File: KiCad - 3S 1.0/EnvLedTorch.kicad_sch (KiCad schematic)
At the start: 64 parts, among them J1 USB_C_Receptacle_USB2.0, J101 Conn_01x02, J102 Conn_01x02, Q1 BSP89, Q2 BSP89, Q3 BSP89, Q4 AO3401A, Q5 AO3401A, SW101 SW_SPST, U1 HY2213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

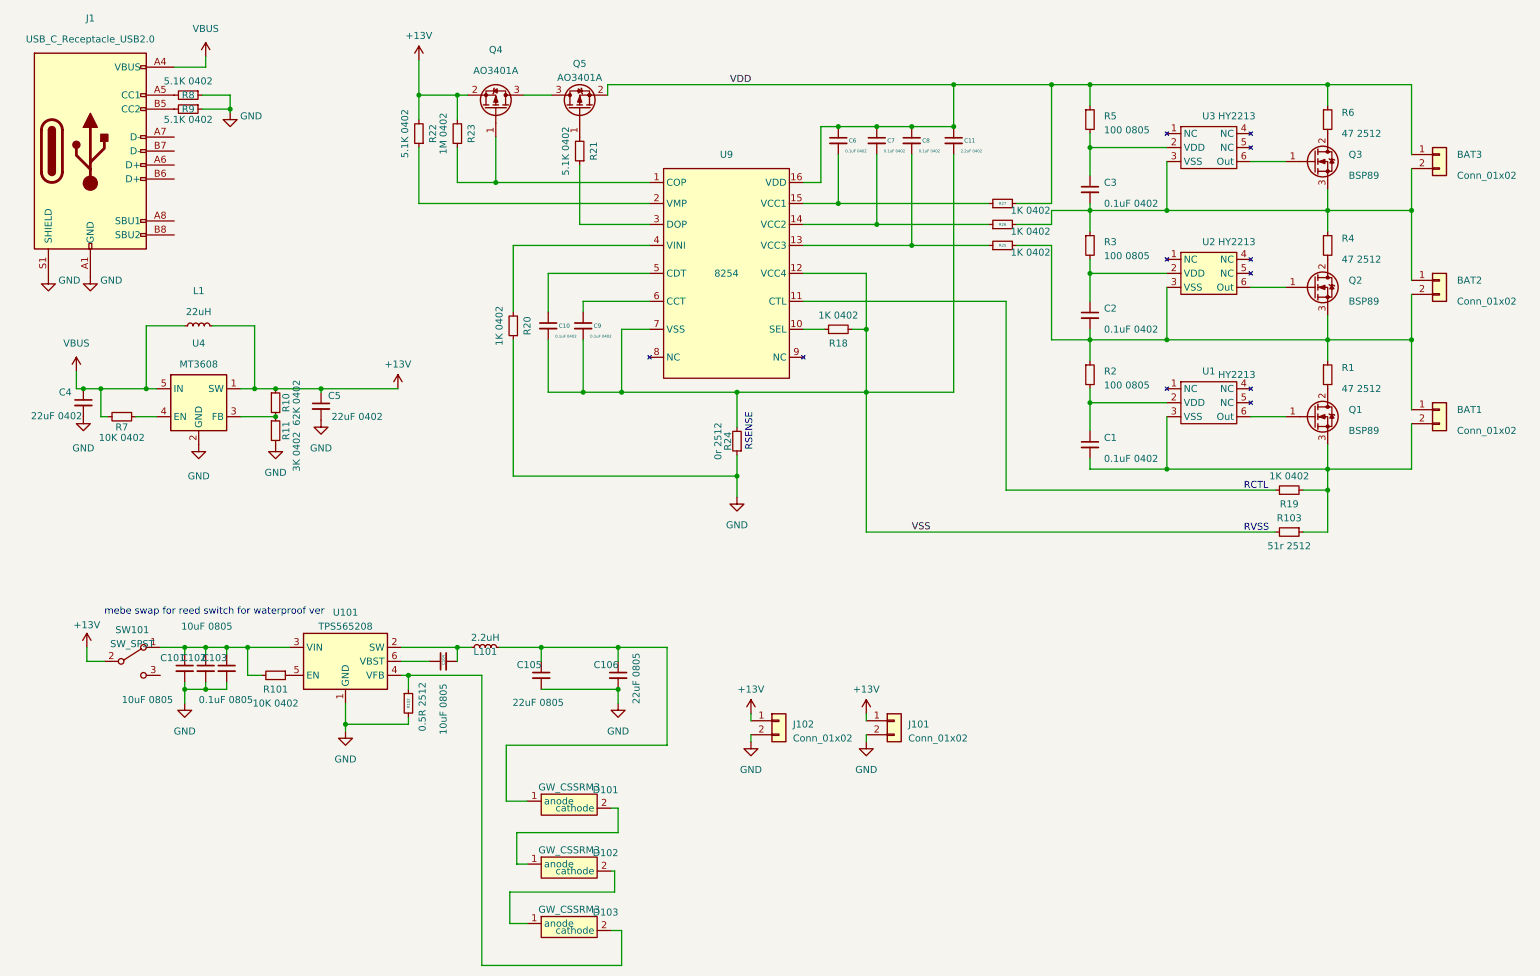
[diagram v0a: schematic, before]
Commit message: created lower cost single cell variant with less leds, this version will draw 1.2A possibly more due to losses and what not but can charge at 1.5A
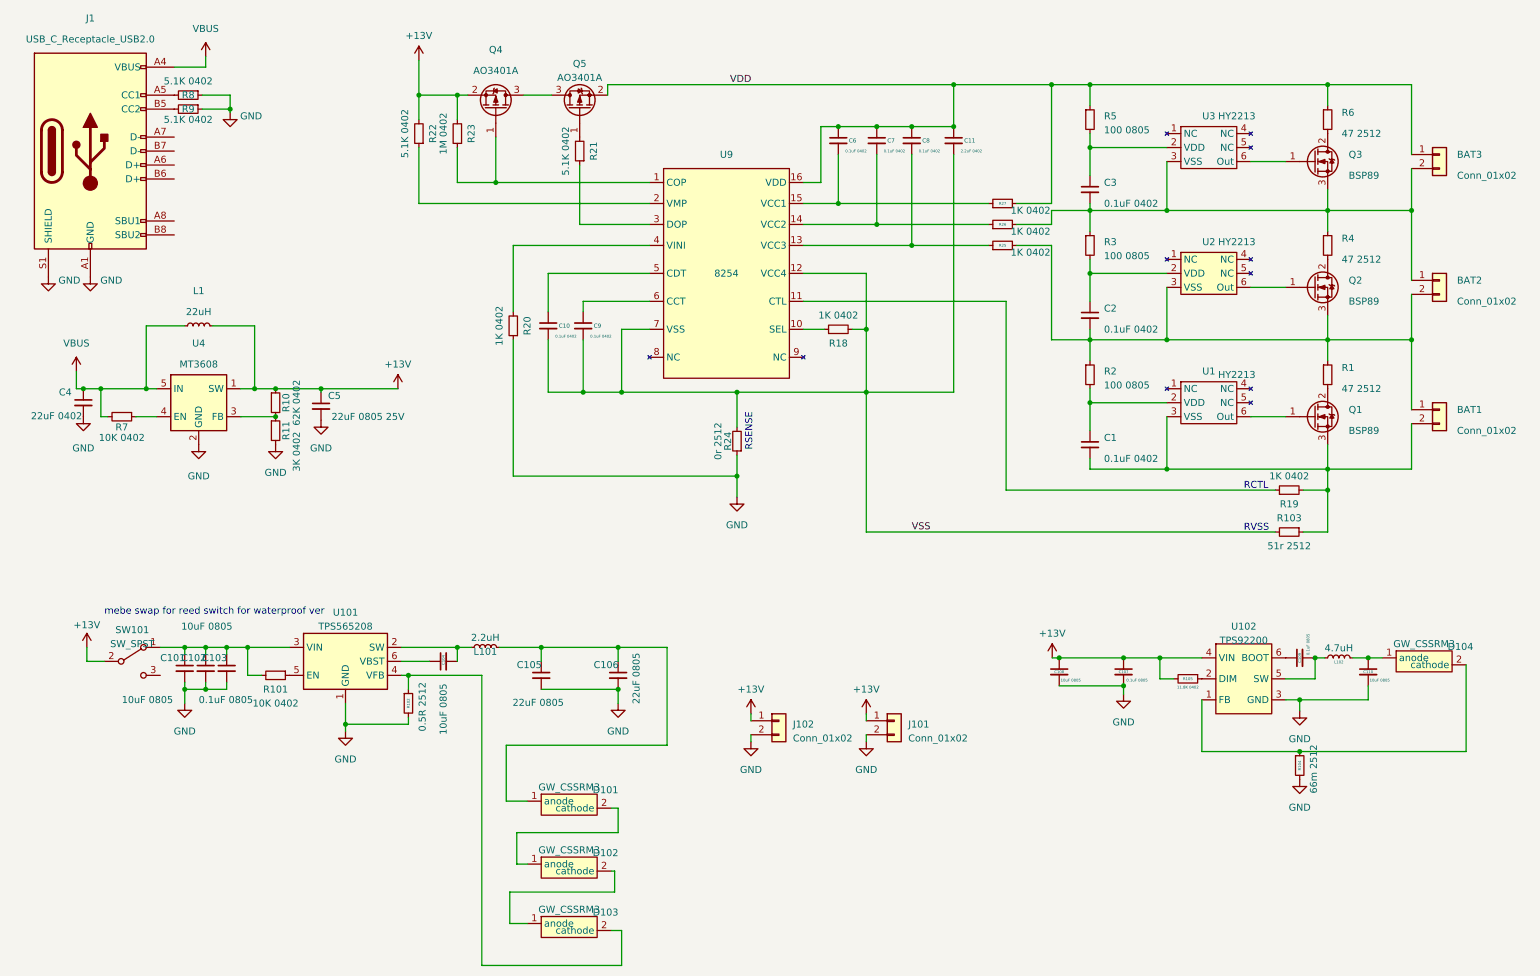
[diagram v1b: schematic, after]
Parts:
- added C107, C109: 0.1uF 0805, Capacitor_SMD:C_0805_2012Metric, symbol Device:C_Small
- added C108, C110: 10uF 0805, Capacitor_SMD:C_0805_2012Metric, symbol Device:C_Small
- added D104: GW_CSSRM3, GW_CSSRM3:GW_CSSRM3, symbol GW CSSRM3:GW_CSSRM3
- added L102: 4.7uH, Inductor_SMD:L_Sunlord_MWSA0402S, symbol Device:L_Small
- added R104: 66m 2512, Resistor_SMD:R_2512_6332Metric, symbol Device:R_Small
- added R105: 11.8K 0402, Resistor_SMD:R_0402_1005Metric, symbol Device:R_Small
- added U102: TPS92200, Package_TO_SOT_SMD:SOT-23-6, symbol TPS92200:TPS92200
- C5: value 22uF 0402 -> 22uF 0805 25V; footprint Capacitor_SMD:C_0402_1005Metric -> Capacitor_SMD:C_0805_2012Metric
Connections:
- net +12V: now also C107.1, C108.1, R105.2, U102.4 (VIN)
- net GND: now also C107.2, C108.2, C110.2, R104.2, U102.3 (GND)
- new net: C109.2, L102.1, U102.5 (SW)
- new net: C110.1, D104.1 (anode), L102.2
- new net: R105.1, U102.2 (DIM)
- new net: D104.2 (cathode), R104.1, U102.1 (FB)
- new net: C109.1, U102.6 (BOOT)
